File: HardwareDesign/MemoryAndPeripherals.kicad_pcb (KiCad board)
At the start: 2 copper layers, 150 x 90 mm, 2 parts

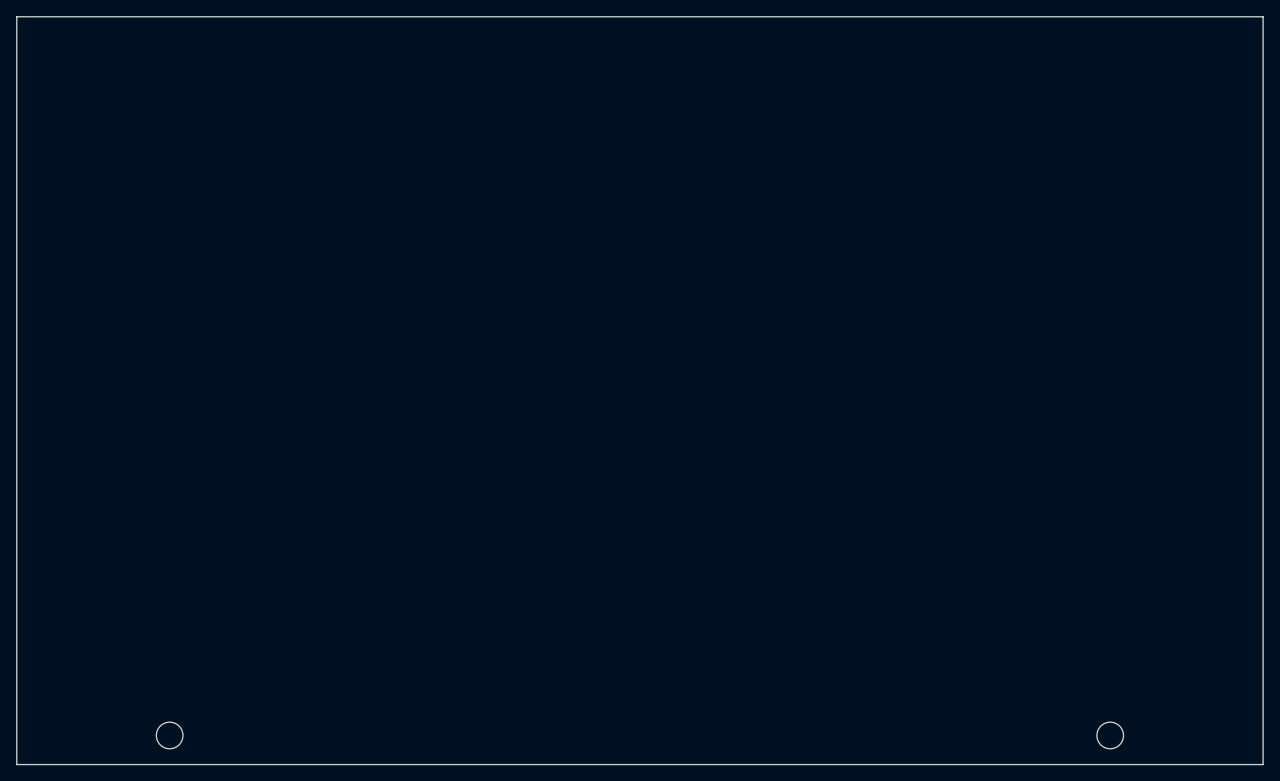
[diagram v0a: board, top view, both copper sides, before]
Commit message: laid out the components
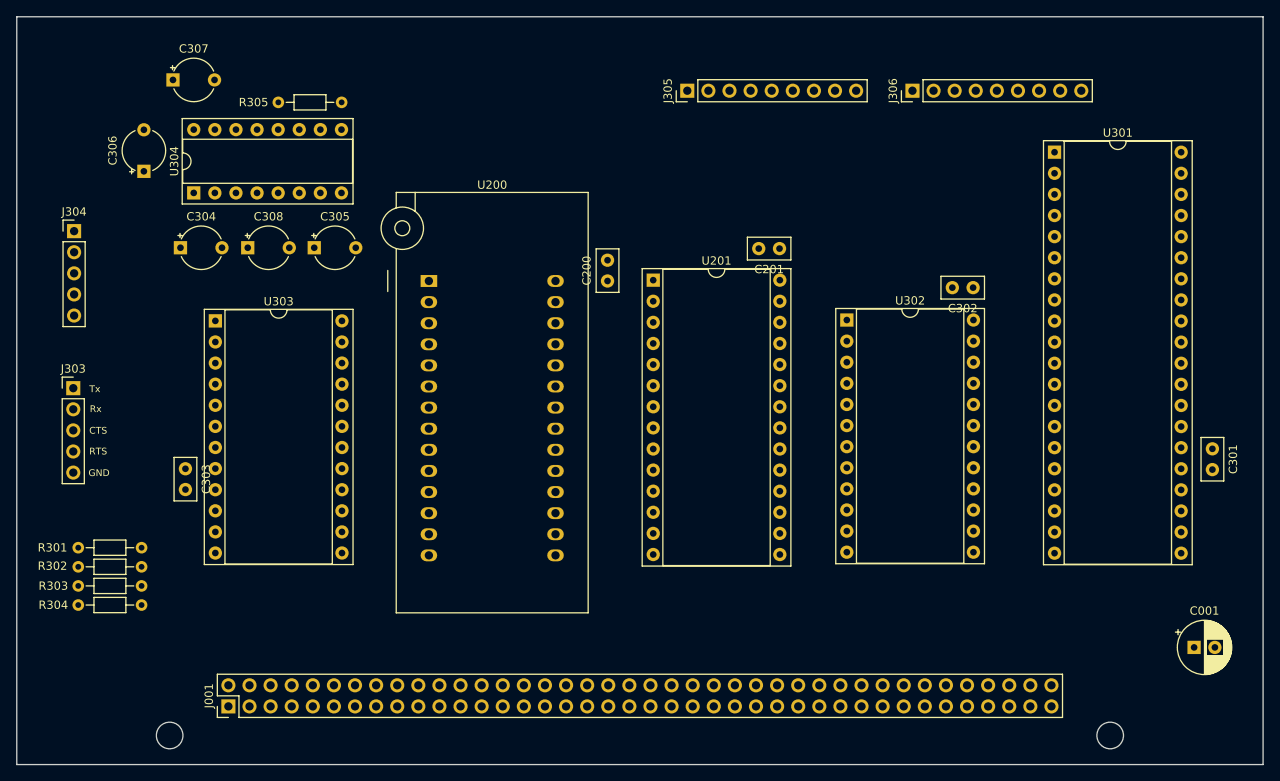
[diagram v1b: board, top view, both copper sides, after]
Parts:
- added C001: 10μF, Capacitor_THT:CP_Radial_D6.3mm_P2.50mm, F.Cu at (141.7, 75.9)
- added C200: 0.1 uF, Capacitor_THT:C_Disc_D5.0mm_W2.5mm_P2.50mm, F.Cu at (71.1, 31.8)
- added C201: 0.1 uF, Capacitor_THT:C_Disc_D5.0mm_W2.5mm_P2.50mm, F.Cu at (91.8, 27.9)
- added C301: 0.1 μF, Capacitor_THT:C_Disc_D5.0mm_W2.5mm_P2.50mm, F.Cu at (143.9, 52.0)
- added C302: 0.1 μF, Capacitor_THT:C_Disc_D5.0mm_W2.5mm_P2.50mm, F.Cu at (115.1, 32.6)
- added C303: 0.1 μF, Capacitor_THT:C_Disc_D5.0mm_W2.5mm_P2.50mm, F.Cu at (20.3, 54.4)
- added C304: 1μF, Capacitor_THT:CP_Radial_Tantal_D5.0mm_P5.00mm, F.Cu at (19.7, 27.8)
- added C305: 1μF, Capacitor_THT:CP_Radial_Tantal_D5.0mm_P5.00mm, F.Cu at (35.8, 27.8)
- added C306: 1μF, Capacitor_THT:CP_Radial_Tantal_D5.0mm_P5.00mm, F.Cu at (15.3, 18.6)
- added C307: 1μF, Capacitor_THT:CP_Radial_Tantal_D5.0mm_P5.00mm, F.Cu at (18.8, 7.60)
- added C308: 1μF, Capacitor_THT:CP_Radial_Tantal_D5.0mm_P5.00mm, F.Cu at (27.8, 27.8)
- added J001: Conn_02x40_Odd_Even, Connector_PinHeader_2.54mm:PinHeader_2x40_P2.54mm_Vertical, F.Cu at (25.5, 83.0)
- added J303: Conn_01x05, Connector_PinHeader_2.54mm:PinHeader_1x05_P2.54mm_Vertical, F.Cu at (6.80, 44.7)
- added J304: Conn_01x05, Connector_PinHeader_2.54mm:PinHeader_1x05_P2.54mm_Vertical, F.Cu at (6.90, 25.8)
- added J305: Conn_01x09, Connector_PinHeader_2.54mm:PinHeader_1x09_P2.54mm_Vertical, F.Cu at (80.7, 8.90)
- added J306: Conn_01x09, Connector_PinHeader_2.54mm:PinHeader_1x09_P2.54mm_Vertical, F.Cu at (107.8, 8.90)
- added R301: 2k7, Resistor_THT:R_Axial_DIN0204_L3.6mm_D1.6mm_P7.62mm_Horizontal, F.Cu at (7.40, 63.9)
- added R302: 2k7, Resistor_THT:R_Axial_DIN0204_L3.6mm_D1.6mm_P7.62mm_Horizontal, F.Cu at (7.40, 66.2)
- added R303: 2k7, Resistor_THT:R_Axial_DIN0204_L3.6mm_D1.6mm_P7.62mm_Horizontal, F.Cu at (7.40, 68.5)
- added R304: 2k7, Resistor_THT:R_Axial_DIN0204_L3.6mm_D1.6mm_P7.62mm_Horizontal, F.Cu at (7.40, 70.8)
- added R305: 10k, Resistor_THT:R_Axial_DIN0204_L3.6mm_D1.6mm_P7.62mm_Horizontal, F.Cu at (39.1, 10.3)
- added U200: 28C256, Socket:DIP_Socket-28_W11.9_W12.7_W15.24_W17.78_W18.5_3M_228-1277-00-0602J, F.Cu at (49.6, 31.8)
- added U201: HM62256BLP-7SL, Package_DIP:DIP-28_W15.24mm_Socket, F.Cu at (76.6, 31.7)
- added U301: 82C55A, Package_DIP:DIP-40_W15.24mm_Socket, F.Cu at (124.9, 16.3)
- added U302: 82C54, Package_DIP:DIP-24_W15.24mm_Socket, F.Cu at (99.9, 36.5)
- added U303: MC6850, Package_DIP:DIP-24_W15.24mm_Socket, F.Cu at (23.9, 36.6)
- added U304: MAX232CPE, Package_DIP:DIP-16_W7.62mm_Socket, F.Cu at (21.3, 21.2)
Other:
- board text added: "CTS"
- board text added: "GND"
- board text added: "RTS"
- board text added: "Rx"
- board text added: "Tx"

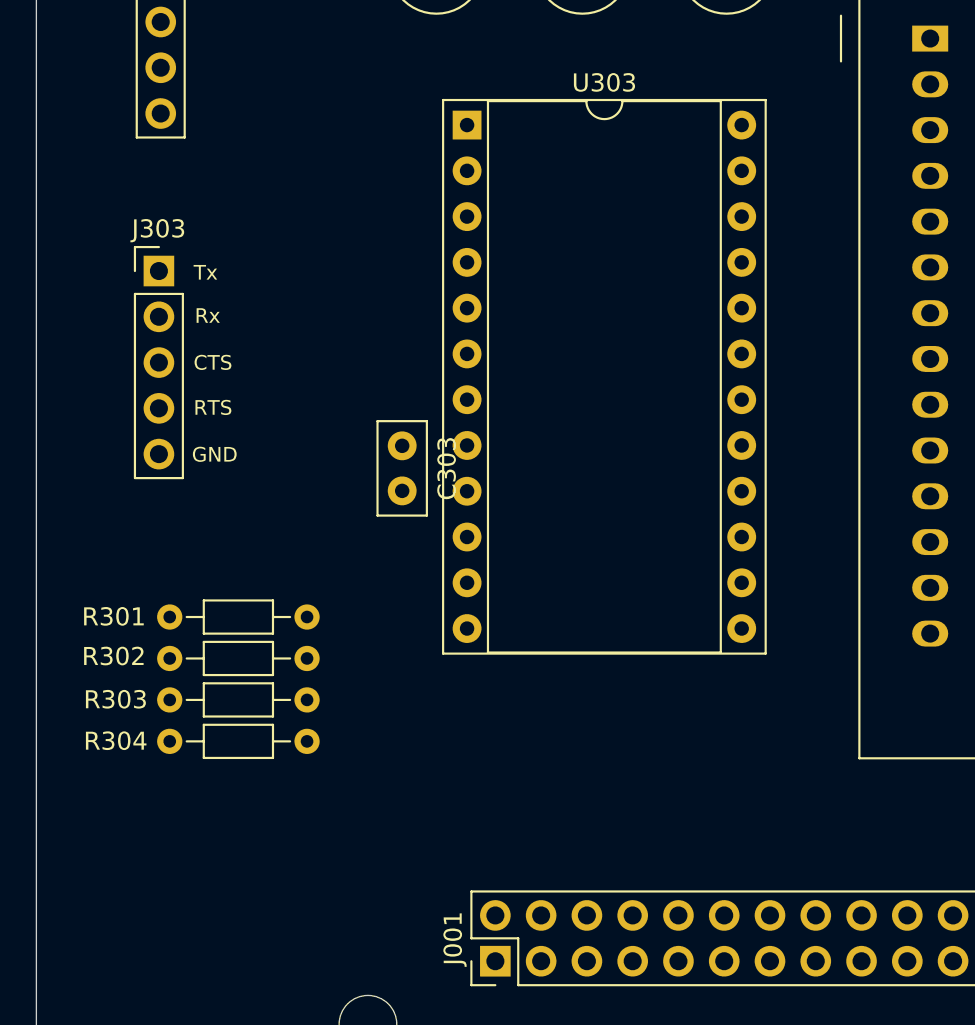
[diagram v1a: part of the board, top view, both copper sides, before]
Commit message: starting to route traces
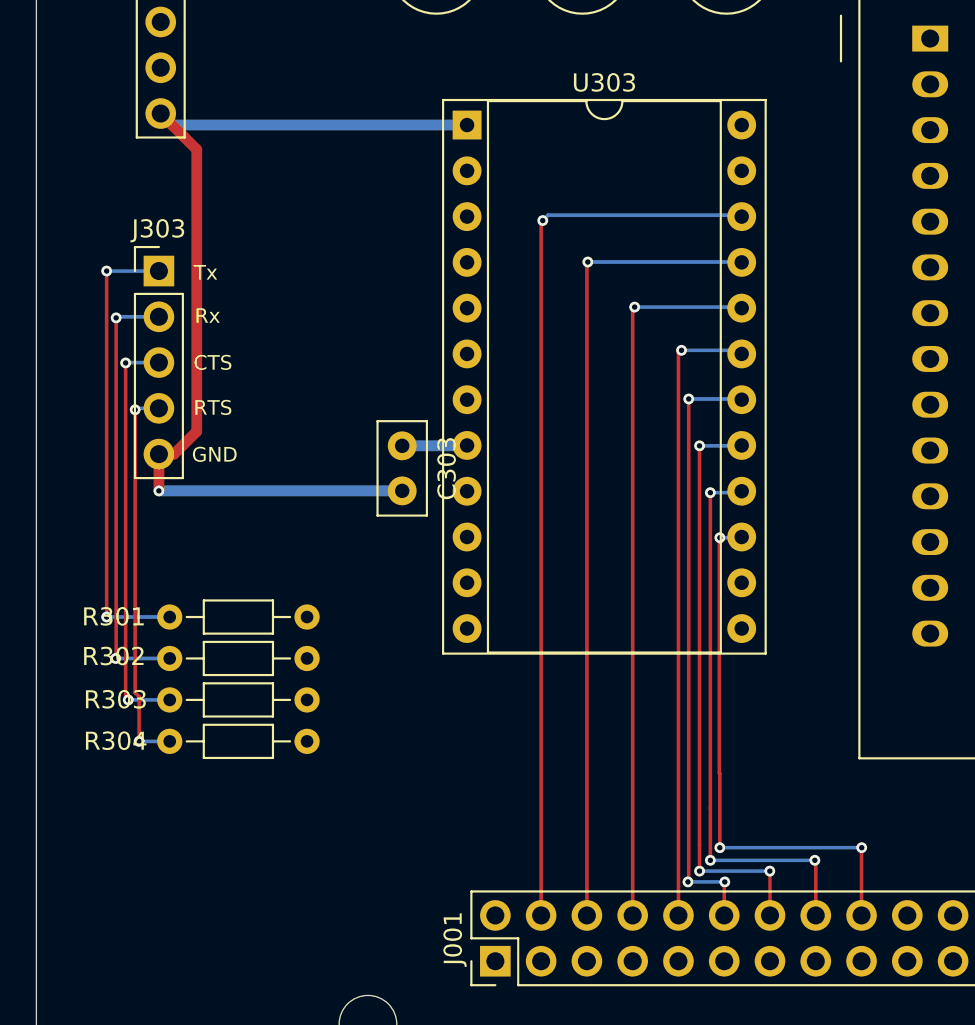
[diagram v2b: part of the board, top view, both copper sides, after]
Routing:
- net GND: track 0.00 -> 53.9 mm, vias 0 -> 1
- net /D0: track 0.00 -> 49.8 mm, vias 0 -> 1
- net /D1: track 0.00 -> 44.8 mm, vias 0 -> 1
- net /D2: track 0.00 -> 39.8 mm, vias 0 -> 1
- net /D3: track 0.00 -> 34.9 mm, vias 0 -> 1
- net /D4: track 0.00 -> 33.6 mm, vias 0 -> 3
- net /D5: track 0.00 -> 32.3 mm, vias 0 -> 3
- net /D6: track 0.00 -> 31.1 mm, vias 0 -> 3
- net /D7: track 0.00 -> 30.1 mm, vias 0 -> 3
- net Net-(J303-Pad1): track 0.00 -> 25.6 mm, vias 0 -> 2
- net Net-(J303-Pad2): track 0.00 -> 24.3 mm, vias 0 -> 2
- net Net-(J303-Pad3): track 0.00 -> 22.9 mm, vias 0 -> 2
- net Net-(J303-Pad4): track 0.00 -> 21.5 mm, vias 0 -> 2
- net VCC: track 0.00 -> 3.61 mm
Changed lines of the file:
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@@
     (thickness 1.6002)
     (drawings 9)
-    (tracks 0)
+    (tracks 101)
     (zones 0)
     (modules 29)
@@
   )
   (setup
-    (last_trace_width 0.127)
+    (last_trace_width 0.6)
     (user_trace_width 0.15)
     (user_trace_width 0.2)
@@
   (gr_line (start 0 90) (end 150 90) (layer Edge.Cuts) (width 0.0381))
   (gr_line (start 0 0) (end 0 90) (layer Edge.Cuts) (width 0.0381))
+  (segment (start 23.88 54.4) (end 23.9 54.38) (width 0.6) (layer Back) (net 1))
+  (segment (start 20.3 54.4) (end 23.88 54.4) (width 0.6) (layer Back) (net 1))
+  (via (at 6.8 56.9) (size 0.6) (drill 0.3) (layers Front Back) (net 2))
+  (segment (start 20.3 56.9) (end 6.8 56.9) (width 0.6) (layer Back) (net 2))
+  (segment (start 6.8 56.9) (end 6.8 54.86) (width 0.6) (layer Front) (net 2))
+  (segment (start 7.54 36.6) (end 6.9 35.96) (width 0.6) (layer Back) (net 2))
+  (segment (start 23.9 36.6) (end 7.54 36.6) (width 0.6) (layer Back) (net 2))
+  (segment (start 8.177001 37.237001) (end 6.9 35.96) (width 0.6) (layer Front) (net 2))
+  (segment (start 8.9 53.6) (end 8.9 37.96) (width 0.6) (layer Front) (net 2))
+  (segment (start 7.64 54.86) (end 8.9 53.6) (width 0.6) (layer Front) (net 2))
+  (segment (start 8.9 37.96) (end 8.177001 37.237001) (width 0.6) (layer Front) (net 2))
+  (segment (start 6.8 54.86) (end 7.64 54.86) (width 0.6) (layer Front) (net 2))
+  (via (at 28.1 41.9) (size 0.6) (drill 0.3) (layers Front Back) (net 6))
+  (segment (start 28.01 41.99) (end 28.1 41.9) (width 0.2) (layer Front) (net 6))
+  (segment (start 28.01 80.46) (end 28.01 41.99) (width 0.2) (layer Front) (net 6))
+  (segment (start 28.1 41.9) (end 28.4 41.6) (width 0.2) (layer Back) (net 6))
+  (segment (start 39.06 41.6) (end 39.14 41.68) (width 0.2) (layer Back) (net 6))
+  (segment (start 28.4 41.6) (end 39.06 41.6) (width 0.2) (layer Back) (net 6))
+  (via (at 30.6 44.2) (size 0.6) (drill 0.3) (layers Front Back) (net 8))
+  (segment (start 30.55 44.25) (end 30.6 44.2) (width 0.2) (layer Front) (net 8))
+  (segment (start 30.55 80.46) (end 30.55 44.25) (width 0.2) (layer Front) (net 8))
+  (segment (start 39.12 44.2) (end 39.14 44.22) (width 0.2) (layer Back) (net 8))
+  (segment (start 30.6 44.2) (end 39.12 44.2) (width 0.2) (layer Back) (net 8))
+  (via (at 33.2 46.7) (size 0.6) (drill 0.3) (layers Front Back) (net 10))
+  (segment (start 33.09 46.81) (end 33.2 46.7) (width 0.2) (layer Front) (net 10))
+  (segment (start 33.09 80.46) (end 33.09 46.81) (width 0.2) (layer Front) (net 10))
+  (segment (start 39.08 46.7) (end 39.14 46.76) (width 0.2) (layer Back) (net 10))
+  (segment (start 33.2 46.7) (end 39.08 46.7) (width 0.2) (layer Back) (net 10))
+  (via (at 35.8 49.1) (size 0.6) (drill 0.3) (layers Front Back) (net 12))
+  (segment (start 35.63 49.27) (end 35.8 49.1) (width 0.2) (layer Front) (net 12))
+  (segment (start 35.63 80.46) (end 35.63 49.27) (width 0.2) (layer Front) (net 12))
+  (segment (start 38.94 49.1) (end 39.14 49.3) (width 0.2) (layer Back) (net 12))
+  (segment (start 35.8 49.1) (end 38.94 49.1) (width 0.2) (layer Back) (net 12))
+  (via (at 36.2 51.8) (size 0.6) (drill 0.3) (layers Front Back) (net 14))
+  (segment (start 36.2 78.49) (end 36.2 51.8) (width 0.2) (layer Front) (net 14))
+  (segment (start 39.1 51.8) (end 39.14 51.84) (width 0.2) (layer Back) (net 14))
+  (segment (start 36.2 51.8) (end 39.1 51.8) (width 0.2) (layer Back) (net 14))
+  (via (at 38.2 78.6) (size 0.6) (drill 0.3) (layers Front Back) (net 14))
+  (segment (start 38.17 78.63) (end 38.2 78.6) (width 0.2) (layer Front) (net 14))
+  (segment (start 38.17 80.46) (end 38.17 78.63) (width 0.2) (layer Front) (net 14))
+  (via (at 36.157 78.6) (size 0.6) (drill 0.3) (layers Front Back) (net 14))
+  (segment (start 38.2 78.6) (end 36.157 78.6) (width 0.2) (layer Back) (net 14))
+  (via (at 36.8 54.4) (size 0.6) (drill 0.3) (layers Front Back) (net 16))
+  (segment (start 36.8 76.55) (end 36.8 54.4) (width 0.2) (layer Front) (net 16))
+  (segment (start 39.12 54.4) (end 39.14 54.38) (width 0.2) (layer Back) (net 16))
+  (segment (start 36.8 54.4) (end 39.12 54.4) (width 0.2) (layer Back) (net 16))
+  (via (at 40.7 78) (size 0.6) (drill 0.3) (layers Front Back) (net 16))
+  (segment (start 40.71 78.01) (end 40.7 78) (width 0.2) (layer Front) (net 16))
+  (segment (start 40.71 80.46) (end 40.71 78.01) (width 0.2) (layer Front) (net 16))
+  (via (at 36.8 78) (size 0.6) (drill 0.3) (layers Front Back) (net 16))
+  (segment (start 40.7 78) (end 36.8 78) (width 0.2) (layer Back) (net 16))
+  (segment (start 36.8 78) (end 36.8 76.55) (width 0.2) (layer Front) (net 16))
+  (via (at 37.4 57) (size 0.6) (drill 0.3) (layers Front Back) (net 18))
+  (segment (start 37.4 74.5) (end 37.4 57) (width 0.2) (layer Front) (net 18))
+  (segment (start 39.06 57) (end 39.14 56.92) (width 0.2) (layer Back) (net 18))
+  (segment (start 37.4 57) (end 39.06 57) (width 0.2) (layer Back) (net 18))
+  (via (at 43.2 77.4) (size 0.6) (drill 0.3) (layers Front Back) (net 18))
+  (segment (start 43.25 77.45) (end 43.2 77.4) (width 0.2) (layer Front) (net 18))
+  (segment (start 43.25 80.46) (end 43.25 77.45) (width 0.2) (layer Front) (net 18))
+  (via (at 37.4 77.4) (size 0.6) (drill 0.3) (layers Front Back) (net 18))
+  (segment (start 43.2 77.4) (end 37.4 77.4) (width 0.2) (layer Back) (net 18))
+  (segment (start 37.4 77.4) (end 37.4 74.5) (width 0.2) (layer Front) (net 18))
+  (via (at 37.927 59.5) (size 0.6) (drill 0.3) (layers Front Back) (net 20))
+  (segment (start 37.9 59.527) (end 37.927 59.5) (width 0.2) (layer Front) (net 20))
+  (segment (start 37.9 72.57) (end 37.9 59.527) (width 0.2) (layer Front) (net 20))
+  (segment (start 39.1 59.5) (end 39.14 59.46) (width 0.2) (layer Back) (net 20))
+  (segment (start 37.927 59.5) (end 39.1 59.5) (width 0.2) (layer Back) (net 20))
+  (via (at 45.8 76.7) (size 0.6) (drill 0.3) (layers Front Back) (net 20))
+  (segment (start 45.79 76.71) (end 45.8 76.7) (width 0.2) (layer Front) (net 20))
+  (segment (start 45.79 80.46) (end 45.79 76.71) (width 0.2) (layer Front) (net 20))
+  (via (at 37.927 76.7) (size 0.6) (drill 0.3) (layers Front Back) (net 20))
+  (segment (start 45.8 76.7) (end 37.927 76.7) (width 0.2) (layer Back) (net 20))
+  (segment (start 37.927 72.597) (end 37.9 72.57) (width 0.2) (layer Front) (net 20))
+  (segment (start 37.927 76.7) (end 37.927 72.597) (width 0.2) (layer Front) (net 20))
+  (via (at 3.9 63.9) (size 0.6) (drill 0.3) (layers Front Back) (net 87))
+  (segment (start 7.4 63.9) (end 3.9 63.9) (width 0.2) (layer Back) (net 87))
+  (segment (start 3.9 63.9) (end 3.9 44.7) (width 0.2) (layer Front) (net 87))
+  (via (at 3.9 44.7) (size 0.6) (drill 0.3) (layers Front Back) (net 87))
+  (segment (start 3.9 44.7) (end 6.8 44.7) (width 0.2) (layer Back) (net 87))
+  (segment (start 4.487 47.24) (end 4.427 47.3) (width 0.2) (layer Back) (net 88))
+  (via (at 4.427 47.3) (size 0.6) (drill 0.3) (layers Front Back) (net 88))
+  (segment (start 6.8 47.24) (end 4.487 47.24) (width 0.2) (layer Back) (net 88))
+  (segment (start 4.427 66.173) (end 4.4 66.2) (width 0.2) (layer Front) (net 88))
+  (via (at 4.4 66.2) (size 0.6) (drill 0.3) (layers Front Back) (net 88))
+  (segment (start 4.427 47.3) (end 4.427 66.173) (width 0.2) (layer Front) (net 88))
+  (segment (start 4.4 66.2) (end 7.4 66.2) (width 0.2) (layer Back) (net 88))
+  (via (at 4.954 49.8) (size 0.6) (drill 0.3) (layers Front Back) (net 89))
+  (segment (start 4.974 49.78) (end 4.954 49.8) (width 0.2) (layer Back) (net 89))
+  (segment (start 6.8 49.78) (end 4.974 49.78) (width 0.2) (layer Back) (net 89))
+  (via (at 5.1 68.5) (size 0.6) (drill 0.3) (layers Front Back) (net 89))
+  (segment (start 4.954 68.354) (end 5.1 68.5) (width 0.2) (layer Front) (net 89))
+  (segment (start 4.954 49.8) (end 4.954 68.354) (width 0.2) (layer Front) (net 89))
+  (segment (start 5.1 68.5) (end 7.4 68.5) (width 0.2) (layer Back) (net 89))
+  (via (at 5.481 52.4) (size 0.6) (drill 0.3) (layers Front Back) (net 90))
+  (segment (start 5.561 52.32) (end 5.481 52.4) (width 0.2) (layer Back) (net 90))
+  (segment (start 6.8 52.32) (end 5.561 52.32) (width 0.2) (layer Back) (net 90))
+  (segment (start 5.481 68.101038) (end 5.7 68.320038) (width 0.2) (layer Front) (net 90))
+  (segment (start 5.481 52.4) (end 5.481 68.101038) (width 0.2) (layer Front) (net 90))
+  (via (at 5.7 70.8) (size 0.6) (drill 0.3) (layers Front Back) (net 90))
+  (segment (start 5.7 68.320038) (end 5.7 70.8) (width 0.2) (layer Front) (net 90))
+  (segment (start 5.7 70.8) (end 7.4 70.8) (width 0.2) (layer Back) (net 90))
 )

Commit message: routed more signals
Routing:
- net /CorePeriphs/-CTS: track 0.00 -> 87.9 mm, vias 0 -> 1
- net /A0: track 0.00 -> 87.0 mm, vias 0 -> 3
- net /A8: track 0.00 -> 85.5 mm, vias 0 -> 3
- net /A7: track 0.00 -> 81.3 mm, vias 0 -> 1
- net /A9: track 0.00 -> 79.8 mm, vias 0 -> 1
- net /A14: track 0.00 -> 77.0 mm, vias 0 -> 1
- net /A6: track 0.00 -> 76.2 mm, vias 0 -> 1
- net /A13: track 0.00 -> 75.2 mm, vias 0 -> 1
- net /A12: track 0.00 -> 73.9 mm, vias 0 -> 1
- net /A11: track 0.00 -> 72.7 mm, vias 0 -> 1
- net /A5: track 0.00 -> 71.1 mm, vias 0 -> 1
- net /A10: track 0.00 -> 70.2 mm, vias 0 -> 1
- net /A4: track 0.00 -> 66.2 mm, vias 0 -> 1
- net /A3: track 0.00 -> 62.6 mm
- net /A2: track 0.00 -> 58.8 mm, vias 0 -> 1
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
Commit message: even more traces routed
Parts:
- turned C001 to 180 degrees
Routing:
- net GND: track 53.9 -> 243.7 mm, vias 1 -> 10
- net VCC: track 3.61 -> 186.2 mm, vias 0 -> 4
- net /E: track 0.00 -> 103.5 mm, vias 0 -> 3
- net /D1: track 64.2 -> 121.6 mm, vias 2 -> 3
- net /D7: track 60.3 -> 115.0 mm, vias 4 -> 6
- net /D3: track 64.5 -> 118.4 mm, vias 2 -> 4
- net /D6: track 59.1 -> 113.0 mm, vias 4 -> 6
- net /D5: track 60.9 -> 114.8 mm, vias 4 -> 6
- net /D4: track 62.8 -> 116.5 mm, vias 4 -> 6
- net /D0: track 71.7 -> 123.9 mm
- net /~RMEM~: track 0.00 -> 27.9 mm
- net /D2: track 56.6 -> 74.5 mm, vias 2 -> 4
- net Net-(C305-Pad1): track 0.00 -> 13.5 mm, vias 0 -> 2
- net Net-(C306-Pad1): track 0.00 -> 11.1 mm, vias 0 -> 1
- net Net-(C304-Pad2): track 0.00 -> 7.33 mm
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
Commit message: getting there, more traces routed...
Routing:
- net GND: track 243.7 -> 402.0 mm, vias 10 -> 16
- net VCC: track 186.2 -> 299.9 mm, vias 4 -> 8
- net Net-(U302-Pad10): track 0.00 -> 111.4 mm, vias 0 -> 2
- net /~WMEM~: track 0.00 -> 104.0 mm, vias 0 -> 3
- net /D0: track 123.9 -> 189.9 mm, vias 2 -> 3
- net /~RMEM~: track 27.9 -> 92.5 mm, vias 0 -> 1
- net /D1: track 121.6 -> 182.4 mm, vias 3 -> 4
- net /CorePeriphs/PA0: track 0.00 -> 59.2 mm, vias 0 -> 1
- net /CorePeriphs/PA5: track 0.00 -> 56.1 mm, vias 0 -> 1
- net /CorePeriphs/PA4: track 0.00 -> 55.9 mm, vias 0 -> 1
- net /CorePeriphs/PA7: track 0.00 -> 55.8 mm, vias 0 -> 1
- net /CorePeriphs/PA6: track 0.00 -> 55.7 mm, vias 0 -> 1
- net /CorePeriphs/PA1: track 0.00 -> 54.2 mm, vias 0 -> 1
- net /D7: track 115.0 -> 168.7 mm, vias 6 -> 7
- net /D2: track 74.5 -> 128.0 mm, vias 4 -> 5
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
